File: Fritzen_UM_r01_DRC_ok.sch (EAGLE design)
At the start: 28 parts, among them IC1 7805T, Q1 16MHz, X1 POWERSUPPLY_DC21MMX, X2 Ser_Comm

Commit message: Second release of the PCB and schematic
Corrections made to the PCB  silkcreen and traces (due to clearances and
other issues). Please do not produce any version older than this one.
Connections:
- net +5V: no longer POWER.2
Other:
- note removed: "Arduino(TM) UNO Rev3"
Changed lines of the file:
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@@
 <layer number="91" name="Nets" color="2" fill="1" visible="yes" active="yes"/>
 <layer number="92" name="Busses" color="1" fill="1" visible="yes" active="yes"/>
-<layer number="93" name="Pins" color="2" fill="1" visible="no" active="yes"/>
+<layer number="93" name="Pins" color="2" fill="1" visible="yes" active="yes"/>
 <layer number="94" name="Symbols" color="4" fill="1" visible="yes" active="yes"/>
 <layer number="95" name="Names" color="7" fill="1" visible="yes" active="yes"/>
 <layer number="96" name="Values" color="7" fill="1" visible="yes" active="yes"/>
-<layer number="97" name="Info" color="7" fill="1" visible="no" active="yes"/>
-<layer number="98" name="Guide" color="6" fill="1" visible="no" active="yes"/>
+<layer number="97" name="Info" color="7" fill="1" visible="yes" active="yes"/>
+<layer number="98" name="Guide" color="6" fill="1" visible="yes" active="yes"/>
 <layer number="99" name="SpiceOrder" color="5" fill="1" visible="yes" active="yes"/>
-<layer number="100" name="Muster" color="7" fill="1" visible="no" active="yes"/>
-<layer number="101" name="Patch_Top" color="7" fill="1" visible="no" active="yes"/>
-<layer number="102" name="Vscore" color="7" fill="1" visible="no" active="yes"/>
+<layer number="100" name="Muster" color="7" fill="1" visible="yes" active="yes"/>
+<layer number="101" name="Patch_Top" color="7" fill="1" visible="yes" active="yes"/>
+<layer number="102" name="Vscore" color="7" fill="1" visible="yes" active="yes"/>
 <layer number="103" name="tMap" color="7" fill="1" visible="yes" active="yes"/>
-<layer number="104" name="Name" color="7" fill="1" visible="no" active="yes"/>
+<layer number="104" name="Name" color="7" fill="1" visible="yes" active="yes"/>
 <layer number="105" name="tPlate" color="7" fill="1" visible="yes" active="yes"/>
 <layer number="106" name="bPlate" color="7" fill="1" visible="yes" active="yes"/>
 <layer number="107" name="Crop" color="7" fill="1" visible="yes" active="yes"/>
-<layer number="116" name="Patch_BOT" color="7" fill="1" visible="no" active="yes"/>
-<layer number="121" name="_tsilk" color="7" fill="1" visible="no" active="yes"/>
-<layer number="122" name="_bsilk" color="7" fill="1" visible="no" active="yes"/>
+<layer number="116" name="Patch_BOT" color="7" fill="1" visible="yes" active="yes"/>
+<layer number="121" name="_tsilk" color="7" fill="1" visible="yes" active="yes"/>
+<layer number="122" name="_bsilk" color="7" fill="1" visible="yes" active="yes"/>
 <layer number="144" name="Drill_legend" color="7" fill="1" visible="yes" active="yes"/>
-<layer number="151" name="HeatSink" color="7" fill="1" visible="no" active="yes"/>
+<layer number="151" name="HeatSink" color="7" fill="1" visible="yes" active="yes"/>
 <layer number="200" name="200bmp" color="1" fill="10" visible="no" active="no"/>
-<layer number="201" name="201bmp" color="7" fill="1" visible="no" active="yes"/>
-<layer number="202" name="202bmp" color="7" fill="1" visible="no" active="yes"/>
-<layer number="203" name="203bmp" color="7" fill="1" visible="no" active="yes"/>
-<layer number="204" name="204bmp" color="7" fill="1" visible="no" active="yes"/>
-<layer number="205" name="205bmp" color="7" fill="1" visible="no" active="yes"/>
-<layer number="206" name="206bmp" color="7" fill="1" visible="no" active="yes"/>
-<layer number="207" name="207bmp" color="7" fill="1" visible="no" active="yes"/>
-<layer number="208" name="208bmp" color="7" fill="1" visible="no" active="yes"/>
-<layer number="209" name="209bmp" color="7" fill="1" visible="no" active="yes"/>
-<layer number="210" name="210bmp" color="7" fill="1" visible="no" active="yes"/>
-<layer number="211" name="211bmp" color="7" fill="1" visible="no" active="yes"/>
-<layer number="212" name="212bmp" color="7" fill="1" visible="no" active="yes"/>
-<layer number="213" name="213bmp" color="7" fill="1" visible="no" active="yes"/>
-<layer number="214" name="214bmp" color="7" fill="1" visible="no" active="yes"/>
+<layer number="201" name="201bmp" color="7" fill="1" visible="yes" active="yes"/>
+<layer number="202" name="202bmp" color="7" fill="1" visible="yes" active="yes"/>
+<layer number="203" name="203bmp" color="7" fill="1" visible="yes" active="yes"/>
+<layer number="204" name="204bmp" color="7" fill="1" visible="yes" active="yes"/>
+<layer number="205" name="205bmp" color="7" fill="1" visible="yes" active="yes"/>
+<layer number="206" name="206bmp" color="7" fill="1" visible="yes" active="yes"/>
+<layer number="207" name="207bmp" color="7" fill="1" visible="yes" active="yes"/>
+<layer number="208" name="208bmp" color="7" fill="1" visible="yes" active="yes"/>
+<layer number="209" name="209bmp" color="7" fill="1" visible="yes" active="yes"/>
+<layer number="210" name="210bmp" color="7" fill="1" visible="yes" active="yes"/>
+<layer number="211" name="211bmp" color="7" fill="1" visible="yes" active="yes"/>
+<layer number="212" name="212bmp" color="7" fill="1" visible="yes" active="yes"/>
+<layer number="213" name="213bmp" color="7" fill="1" visible="yes" active="yes"/>
+<layer number="214" name="214bmp" color="7" fill="1" visible="yes" active="yes"/>
 <layer number="215" name="215bmp" color="16" fill="1" visible="yes" active="yes"/>
 <layer number="216" name="216bmp" color="17" fill="1" visible="yes" active="yes"/>
@@
 <layer number="250" name="Descript" color="3" fill="1" visible="no" active="no"/>
 <layer number="251" name="SMDround" color="12" fill="11" visible="no" active="no"/>
-<layer number="254" name="cooling" color="7" fill="1" visible="no" active="yes"/>
+<layer number="254" name="cooling" color="7" fill="1" visible="yes" active="yes"/>
 </layers>
 <schematic>
@@
 <text x="227.965" y="82.55" size="1.778" layer="91">12</text>
 <text x="227.965" y="85.09" size="1.778" layer="91">13</text>
-<text x="-61.595" y="127" size="6.4516" layer="91">Arduino(TM) UNO Rev3</text>
 <text x="226.06" y="93.98" size="1.778" layer="91">SDA</text>
 <text x="226.06" y="96.52" size="1.778" layer="91">SCL</text>
@@
 <segment>
 <wire x1="132.08" y1="129.54" x2="132.08" y2="139.7" width="0.1524" layer="91"/>
-<wire x1="154.94" y1="129.54" x2="147.32" y2="129.54" width="0.1524" layer="91"/>
-<wire x1="147.32" y1="129.54" x2="132.08" y2="129.54" width="0.1524" layer="91"/>
-<wire x1="154.94" y1="137.16" x2="147.32" y2="137.16" width="0.1524" layer="91"/>
-<wire x1="147.32" y1="137.16" x2="147.32" y2="129.54" width="0.1524" layer="91"/>
-<junction x="147.32" y="129.54"/>
+<wire x1="154.94" y1="129.54" x2="132.08" y2="129.54" width="0.1524" layer="91"/>
 <pinref part="P+4" gate="1" pin="+5V"/>
 <pinref part="POWER" gate="A" pin="5"/>
-<pinref part="POWER" gate="A" pin="2"/>
 </segment>
 <segment>

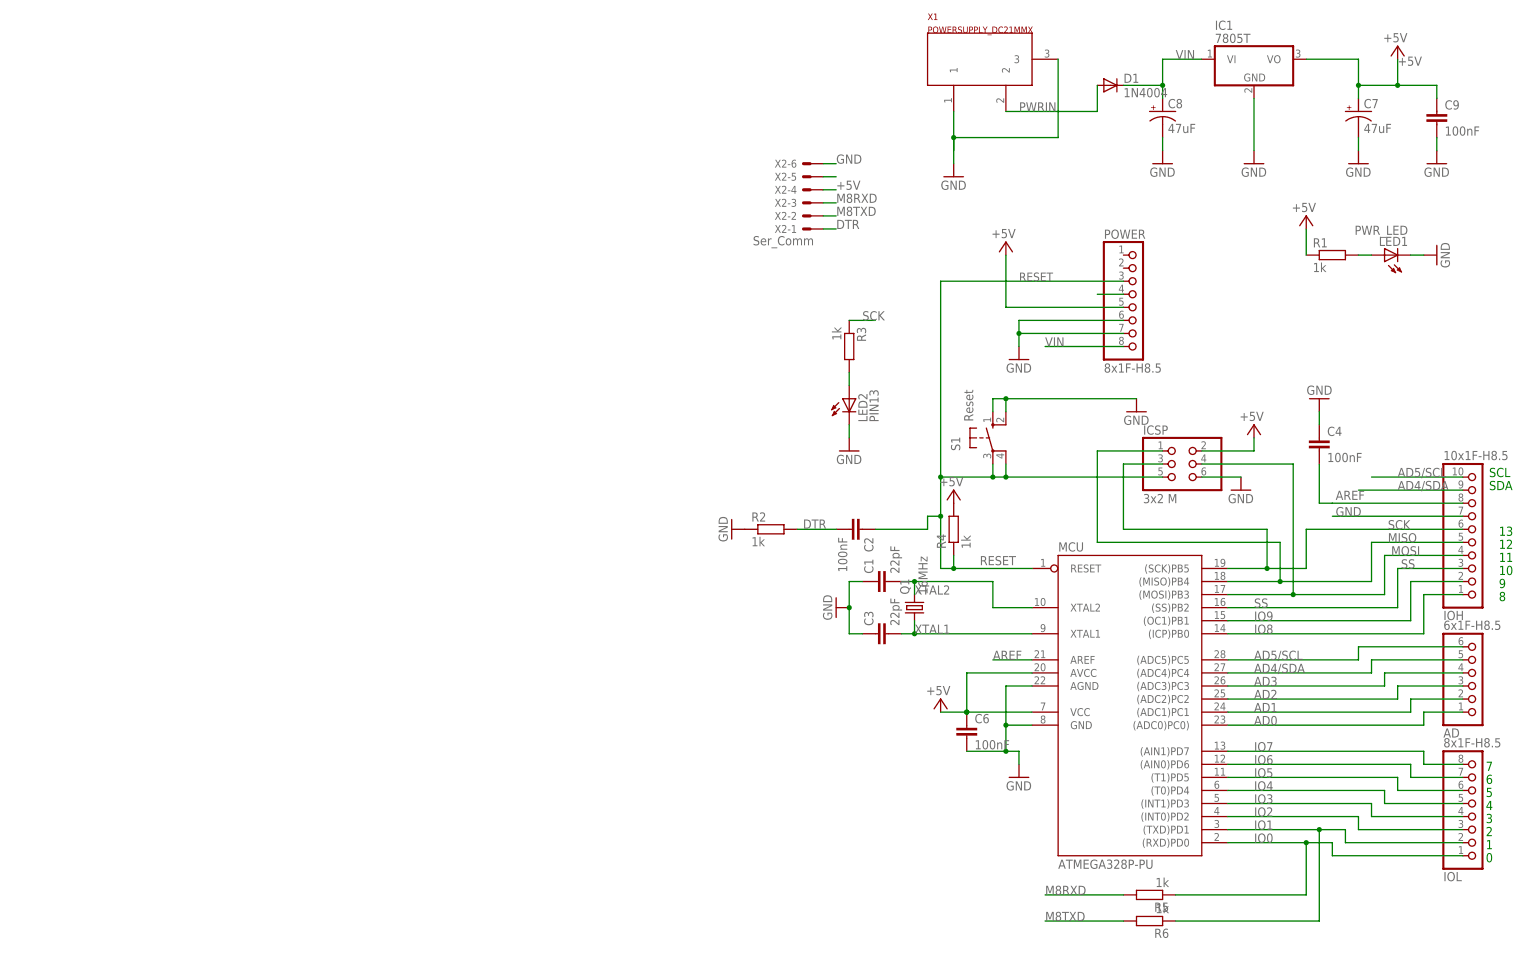
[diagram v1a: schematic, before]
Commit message: Cleaning PCB and Fabrication files
I have order 30 pieces of this board revision at MakerStudio.cc
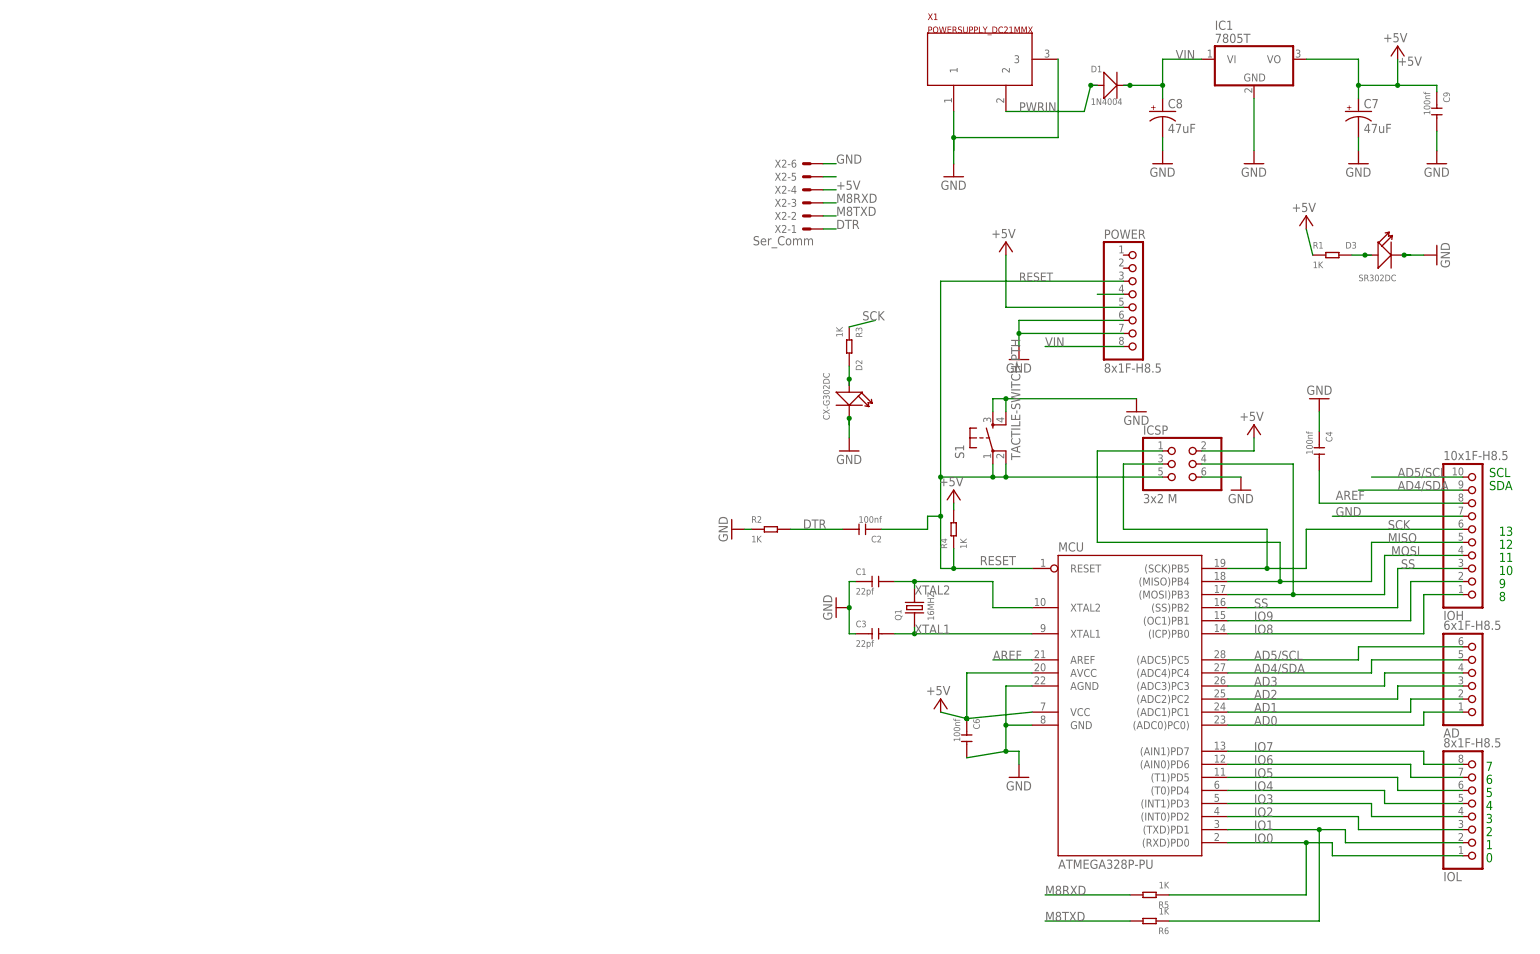
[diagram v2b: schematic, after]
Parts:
- removed LED1: PWR_LED, led:LED3MM
- removed LED2: PIN13, led:LED5MM
- added D2: CX-G302DC, Seeed-OPL-Diode:DIP-LED-GREEN-GREEN(2P-D3MM)
- added D3: SR302DC, Seeed-OPL-Diode:DIP-LED-RED-RED(2P-D3MM)
- C1, C3: value 22pF -> 22pf; device capacitor-wima:C2.5/2 -> Seeed-OPL-Capacitor:DIP-CERAMIC-DISC-22PF-50V-10%-NPO(D4.0MM)
- C2, C4, C6, C9: value 100nF -> 100nf; device capacitor-wima:C2,5-3 -> Seeed-OPL-Capacitor:DIP-CERAMIC-DISC-100NF-50V-Y5V(D5.0MM)
- D1: device diode:1N4004 -> Seeed-OPL-Diode:DIP-DIODE-400V-1A(DO-41)
- Q1: value 16MHz -> 16MHZ; device crystal:CRYSTALHC49S -> Seeed-OPL-Crystal-Oscillator:DIP-CRYSTAL-16MHZ-18PF-30PPM-50R(HC49US)
- R1, R2, R3, R4, R5, R6: value 1k -> 1K; device rcl:R-EU_0207/10 -> Seeed-OPL-Resistor:DIP-RES-1K-5%-1/4W(PR-D2.3XL6.5MM)
- S1: value Reset -> TACTILE-SWITCH-PTH; device switch-omron:10-XX -> GeekAmmo:TACTILE-SWITCH-PTH
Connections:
- net GND: now also D2.-, D3.-, S1.3, S1.4; no longer LED1.C, LED2.C, S1.S, S1.S1
- net N$2: now also D2.+; no longer LED2.A
- net N$3: now also D3.+; no longer LED1.A
- net PWRIN: now also D1.+; no longer D1.A
- net RESET: now also S1.1, S1.2; no longer S1.P, S1.P1
- net VIN: now also D1.-; no longer D1.C
